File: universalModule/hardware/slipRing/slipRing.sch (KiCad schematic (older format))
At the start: 10 parts, among them J1 Conn_01x06_Male, J2 Conn_01x06_Male

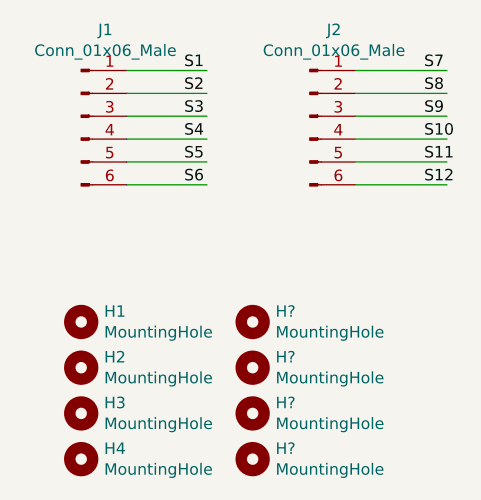
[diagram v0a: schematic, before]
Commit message: Common: Rebrand "Dock" to "RoFICoM"
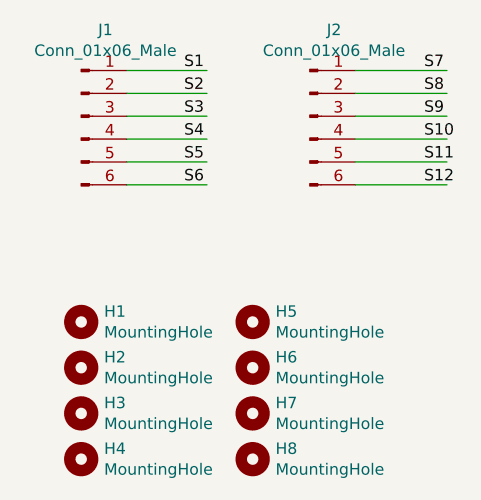
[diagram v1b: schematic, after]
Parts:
- gave numbers to parts that had none: 4
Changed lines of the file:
@@
 $EndComp
 $Comp
-L Mechanical:MountingHole H?
+L Mechanical:MountingHole H5
 U 1 1 5C470271
 P 5250 4150
-F 0 "H?" H 5350 4196 50  0000 L CNN
+F 0 "H5" H 5350 4196 50  0000 L CNN
 F 1 "MountingHole" H 5350 4105 50  0000 L CNN
 F 2 "MountingHole:MountingHole_2.2mm_M2" H 5250 4150 50  0001 C CNN
@@
 $EndComp
 $Comp
-L Mechanical:MountingHole H?
+L Mechanical:MountingHole H6
 U 1 1 5C470277
 P 5250 4350
-F 0 "H?" H 5350 4396 50  0000 L CNN
+F 0 "H6" H 5350 4396 50  0000 L CNN
 F 1 "MountingHole" H 5350 4305 50  0000 L CNN
 F 2 "MountingHole:MountingHole_2.2mm_M2" H 5250 4350 50  0001 C CNN
@@
 $EndComp
 $Comp
-L Mechanical:MountingHole H?
+L Mechanical:MountingHole H7
 U 1 1 5C47027D
 P 5250 4550
-F 0 "H?" H 5350 4596 50  0000 L CNN
+F 0 "H7" H 5350 4596 50  0000 L CNN
 F 1 "MountingHole" H 5350 4505 50  0000 L CNN
 F 2 "MountingHole:MountingHole_2.2mm_M2" H 5250 4550 50  0001 C CNN
@@
 $EndComp
 $Comp
-L Mechanical:MountingHole H?
+L Mechanical:MountingHole H8
 U 1 1 5C470283
 P 5250 4750
-F 0 "H?" H 5350 4796 50  0000 L CNN
+F 0 "H8" H 5350 4796 50  0000 L CNN
 F 1 "MountingHole" H 5350 4705 50  0000 L CNN
 F 2 "MountingHole:MountingHole_2.2mm_M2" H 5250 4750 50  0001 C CNN
